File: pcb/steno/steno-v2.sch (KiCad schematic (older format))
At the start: 59 parts, among them J1 Conn_01x02, J2 Conn_01x04, K1 KEYSW, K10 KEYSW, K11 KEYSW, K12 KEYSW, K13 KEYSW, K14 KEYSW, K15 KEYSW, K16 KEYSW, K17 KEYSW, K18 KEYSW, K19 KEYSW, K2 KEYSW, K20 KEYSW, K21 KEYSW, K22 KEYSW, K23 KEYSW, K24 KEYSW, K25 KEYSW, K26 KEYSW, K27 KEYSW, K28 KEYSW, K3 KEYSW, K4 KEYSW, K5 KEYSW, K6 KEYSW, K7 KEYSW, K8 KEYSW, K9 KEYSW, U1 Adafruit_Feather

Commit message: v2 KiCAD files
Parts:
- added D29, D30: DIODE, Diode_THT:D_DO-34_SOD68_P7.62mm_Horizontal, symbol Simulation_SPICE:DIODE
- added J2: 503182-1852, misc:MOLEX_503182-1852, symbol 503182-1852:503182-1852
- added K29, K30: KEYSW, Keebio-Parts:Kailh-PG1350-1u-No-Clickhole, symbol canadian_parts:KEYSW
- added R1: 10K, Resistor_SMD:R_0805_2012Metric, symbol Device:R
- added U2: MT25QL128ABA1ESE, steno:SOIC-8, symbol steno:MT25QL128ABA1ESE
- renumbered J2 to J3
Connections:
- net labels added: COL10, COL7, COL8, COL9, CS, MISO, MOSI, SCLK
- net labels removed: ROW4, ROW5
- wire segments 127 -> 120
- no-connect marks 6 -> 5
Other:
- moved on the sheet: D1, K1

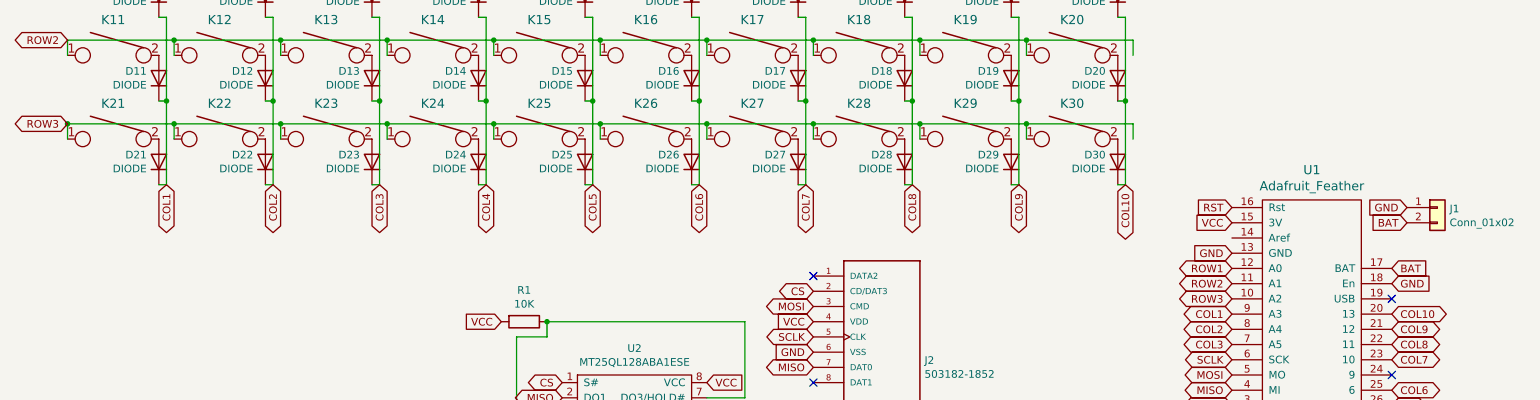
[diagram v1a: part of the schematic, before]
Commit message: Update PCB and footprints
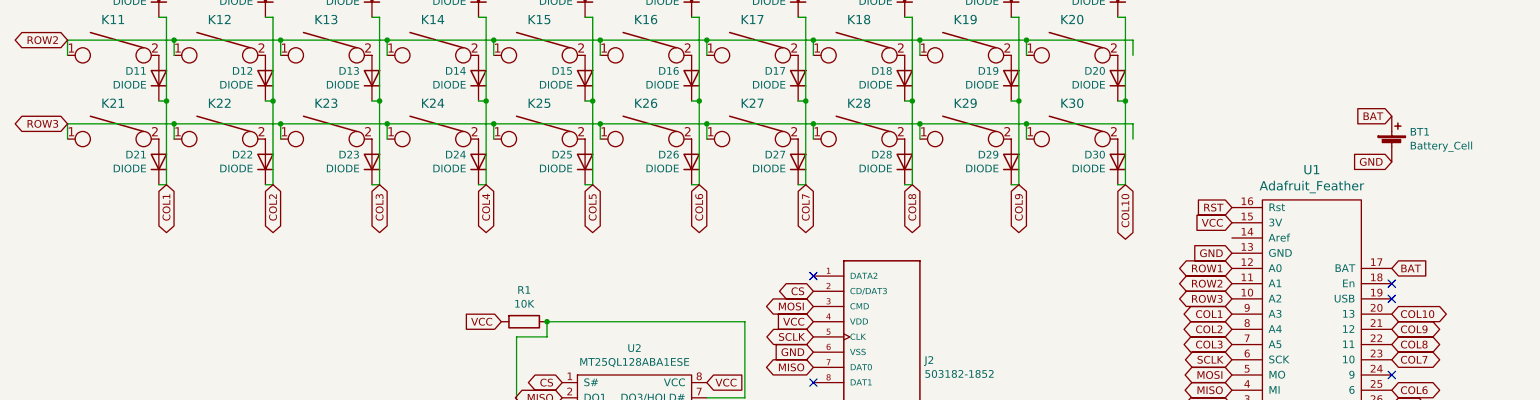
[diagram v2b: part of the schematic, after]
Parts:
- removed J1: Conn_01x02, Connector_JST:JST_PH_B2B-PH-SM4-TB_1x02-1MP_P2.00mm_Vertical, symbol Connector_Generic:Conn_01x02
- added BT1: Battery_Cell, Connector_JST:JST_PH_S2B-PH-SM4-TB_1x02-1MP_P2.00mm_Horizontal, symbol Device:Battery_Cell
- U2: footprint steno:SOIC-8 -> Package_SO:SOP-8_5.28x5.23mm_P1.27mm
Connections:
- no-connect marks 5 -> 6
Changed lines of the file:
@@
 NoConn ~ 9650 5800
 NoConn ~ 10700 4900
-Text GLabel 10700 4800 2    50   Input ~ 0
-GND
-$Comp
-L Connector_Generic:Conn_01x02 J1
-U 1 1 5E6B230F
-P 11000 4300
-F 0 "J1" H 11080 4292 50  0000 L CNN
-F 1 "Conn_01x02" H 11080 4201 50  0000 L CNN
-F 2 "Connector_JST:JST_PH_B2B-PH-SM4-TB_1x02-1MP_P2.00mm_Vertical" H 11000 4300 50  0001 C CNN
-F 3 "~" H 11000 4300 50  0001 C CNN
-	1    11000 4300
-	1    0    0    -1
-$EndComp
-Text GLabel 10800 4300 0    50   Input ~ 0
+Text GLabel 10700 4000 0    50   Input ~ 0
 GND
 Text GLabel 10700 4700 2    50   Input ~ 0
 BAT
-Text GLabel 10800 4400 0    50   Input ~ 0
+Text GLabel 10700 3700 0    50   Input ~ 0
 BAT
 $Comp
@@
 F 0 "U2" H 5725 5875 50  0000 C CNN
 F 1 "MT25QL128ABA1ESE" H 5725 5784 50  0000 C CNN
-F 2 "steno:SOIC-8" H 5650 5150 50  0001 C CNN
+F 2 "Package_SO:SOP-8_5.28x5.23mm_P1.27mm" H 5650 5150 50  0001 C CNN
 F 3 "" H 5650 5150 50  0001 C CNN
 	1    5650 5550
@@
 Wire Wire Line
 	2700 3750 3400 3750
-Connection ~ 2000 3750
+NoConn ~ 10700 4800
+$Comp
+L Device:Battery_Cell BT1
+U 1 1 5EC9EBF8
+P 10700 3900
+F 0 "BT1" H 10818 3996 50  0000 L CNN
+F 1 "Battery_Cell" H 10818 3905 50  0000 L CNN
+F 2 "Connector_JST:JST_PH_S2B-PH-SM4-TB_1x02-1MP_P2.00mm_Horizontal" V 10700 3960 50  0001 C CNN
+F 3 "~" V 10700 3960 50  0001 C CNN
+	1    10700 3900
+	1    0    0    -1
+$EndComp
 $EndSCHEMATC

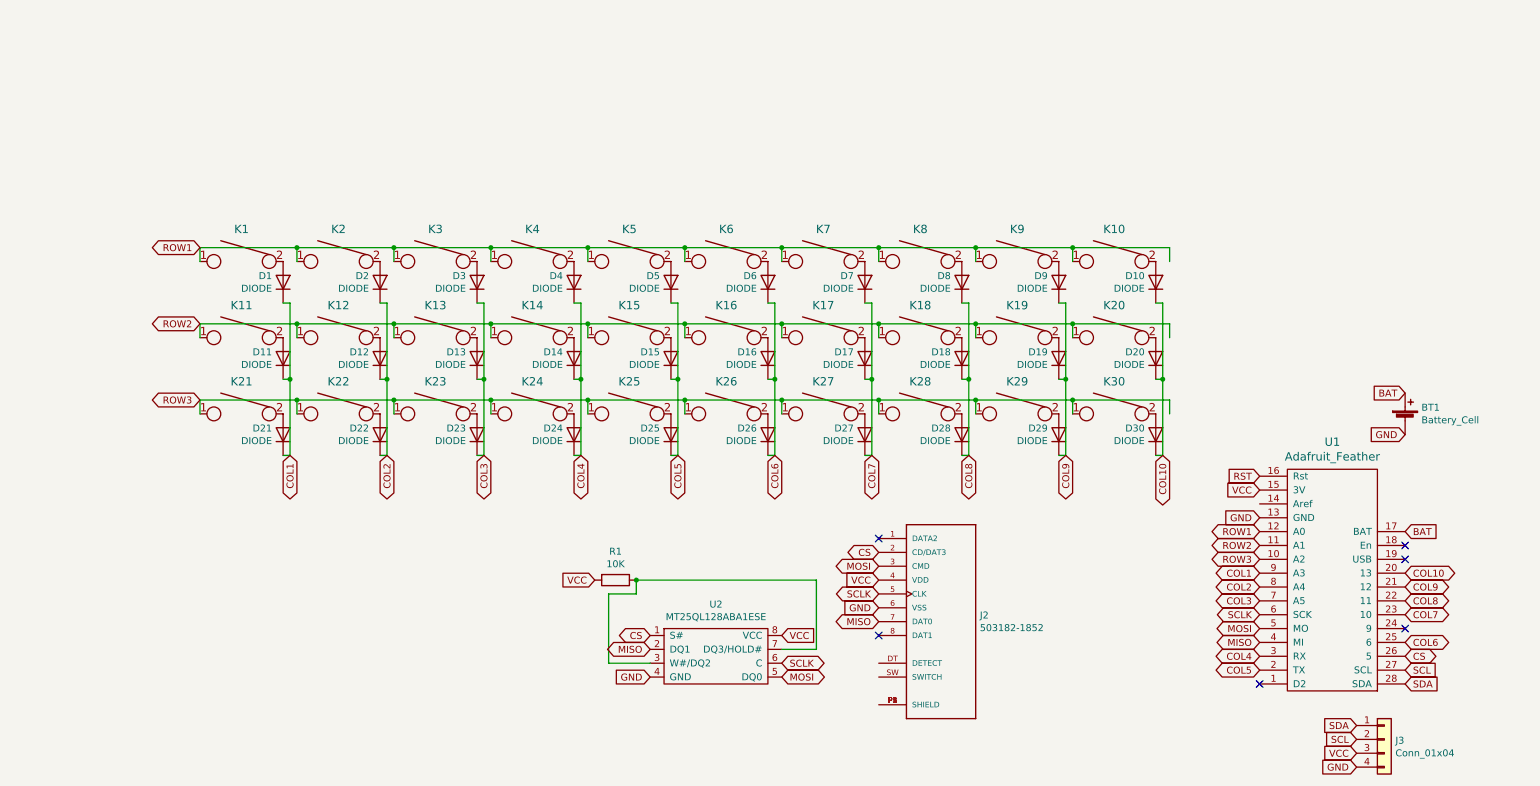
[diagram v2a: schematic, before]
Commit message: v3 component placement; Removed JST connector; Added OLED footprint
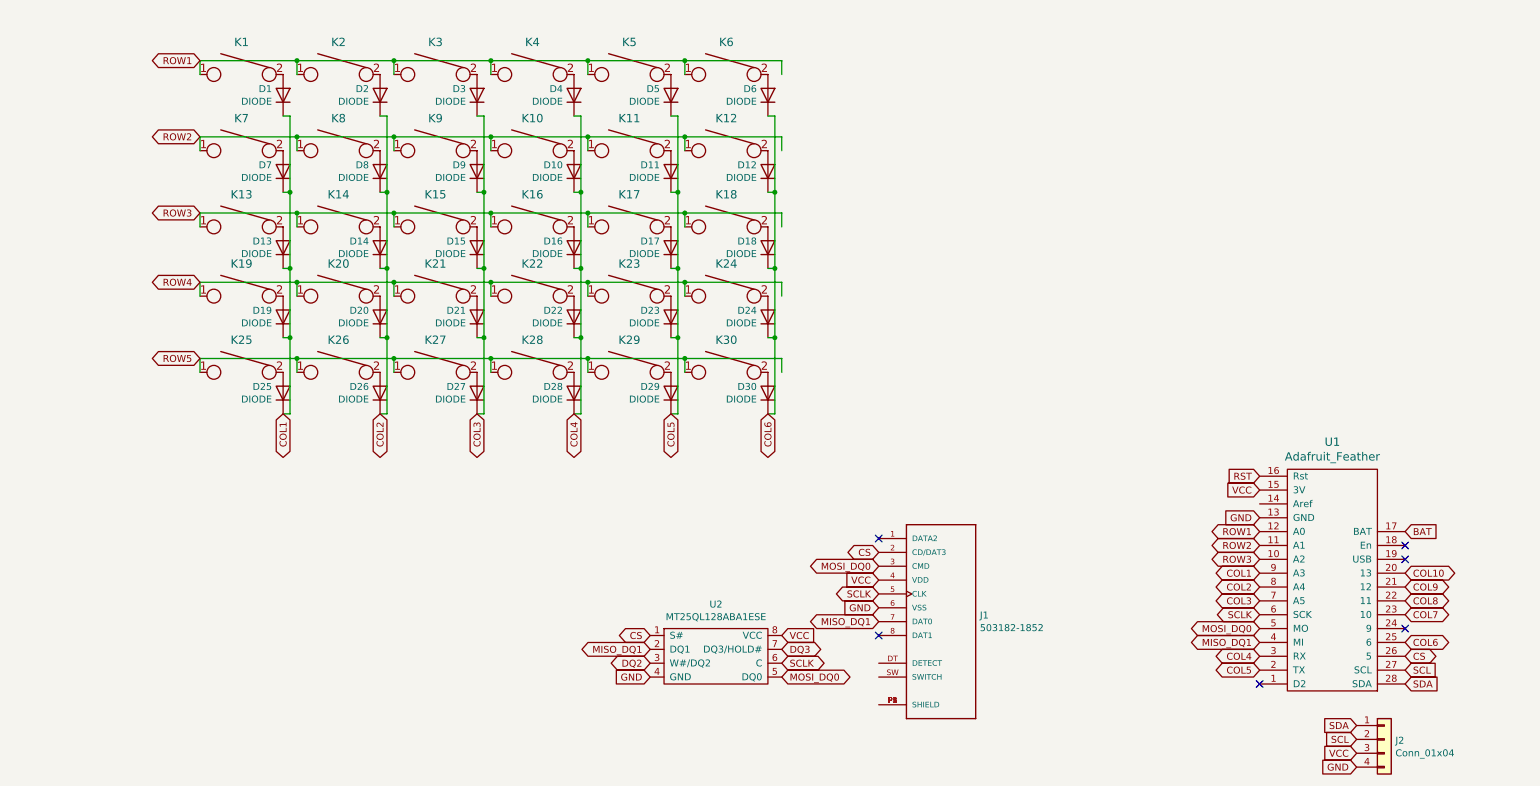
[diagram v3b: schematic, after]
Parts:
- removed BT1: Battery_Cell, Connector_JST:JST_PH_S2B-PH-SM4-TB_1x02-1MP_P2.00mm_Horizontal, symbol Device:Battery_Cell
- removed D10, D16, D17, D7, D8, D9: DIODE, Diode_THT:D_DO-34_SOD68_P7.62mm_Horizontal, symbol Simulation_SPICE:DIODE
- removed K10, K16, K17, K7, K8, K9: KEYSW, Keebio-Parts:Kailh-PG1350-1u-No-Clickhole, symbol canadian_parts:KEYSW
- removed R1: 10K, Resistor_SMD:R_0805_2012Metric, symbol Device:R
- added D12, D21, D22, D23, D24, D25: DIODE, Diode_THT:D_DO-34_SOD68_P7.62mm_Horizontal, symbol Simulation_SPICE:DIODE
- added K12, K21, K22, K23, K24, K25: KEYSW, Keebio-Parts:Kailh-PG1350-1u-No-Clickhole, symbol canadian_parts:KEYSW
- J2: renamed from J3; footprint Connector_PinHeader_2.54mm:PinHeader_1x04_P2.54mm_Vertical -> steno:OLED
- renumbered D14 to D10, D15 to D11, D21 to D13, D22 to D14, D23 to D15, D24 to D16, D25 to D17, D11 to D7, D12 to D8, D13 to D9, J2 to J1, K14 to K10, K15 to K11, K21 to K13, K22 to K14, K23 to K15, K24 to K16, K25 to K17, K11 to K7, K12 to K8, K13 to K9
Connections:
- net labels added: DQ2, DQ3, MISO_DQ1, MOSI_DQ0, ROW4, ROW5
- net labels removed: MISO, MOSI
- wire segments 120 -> 119
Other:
- moved on the sheet: D1, D10, D11, D13, D14, D15, D16, D17, D2, D3, D4, D5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

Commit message: Routed and plotted v3
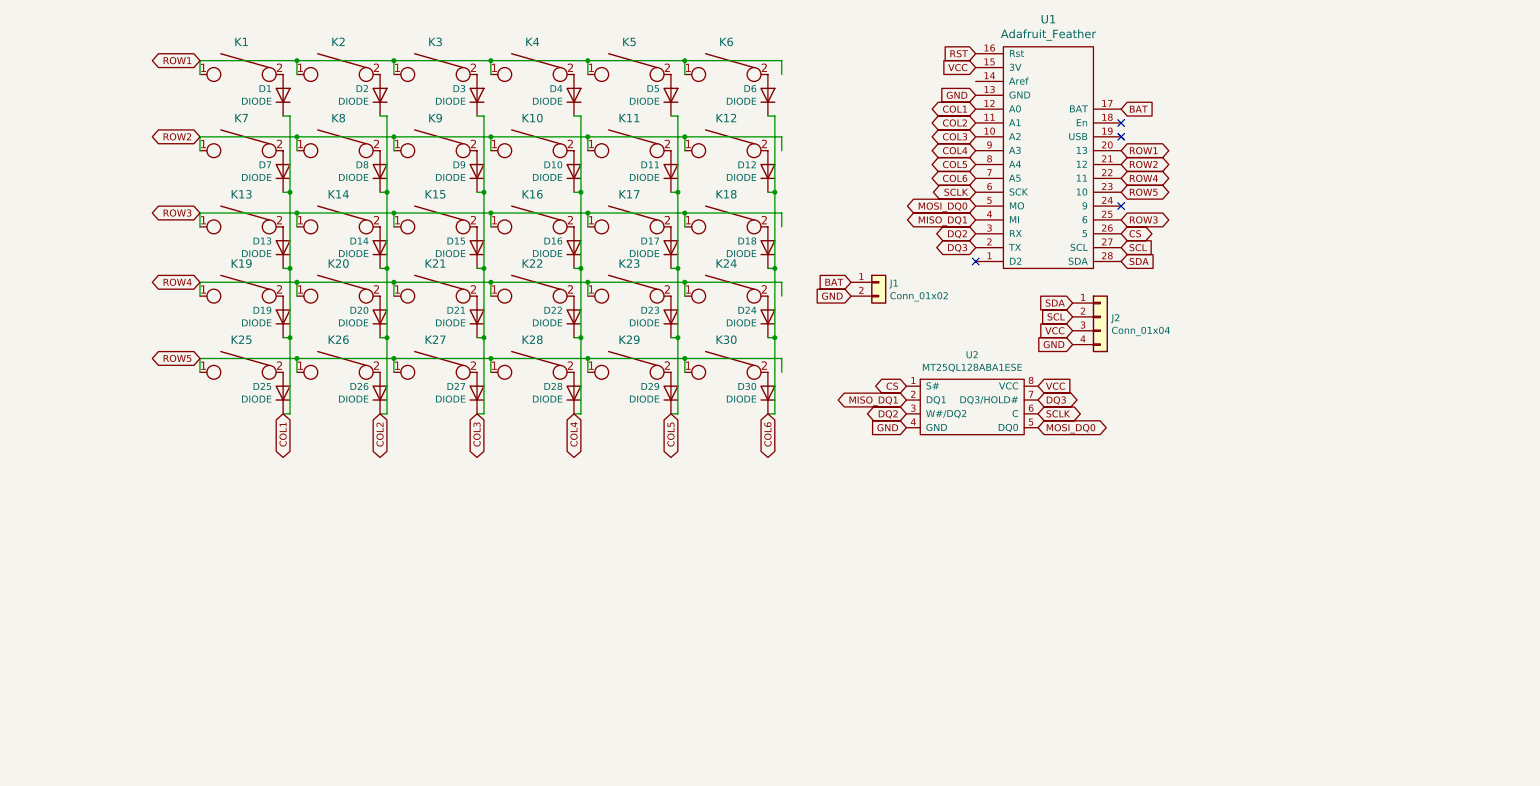
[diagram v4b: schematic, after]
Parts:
- removed J1: 503182-1852, misc:MOLEX_503182-1852, symbol 503182-1852:503182-1852
- added J1: Conn_01x02, Connector_PinHeader_2.54mm:PinHeader_1x02_P2.54mm_Vertical, symbol Connector_Generic:Conn_01x02
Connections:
- net labels removed: COL10, COL7, COL8, COL9
- no-connect marks 6 -> 4
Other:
- moved on the sheet: J2, U1, U2
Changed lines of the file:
@@
 	0    -1   1    0
 $EndComp
-Text GLabel 9650 4600 0    50   Input ~ 0
+Text GLabel 7600 1550 0    50   Input ~ 0
 GND
-Text GLabel 9650 4700 0    50   BiDi ~ 0
+Text GLabel 8650 1950 2    50   BiDi ~ 0
 ROW1
-Text GLabel 9650 4800 0    50   BiDi ~ 0
+Text GLabel 8650 2050 2    50   BiDi ~ 0
 ROW2
-Text GLabel 9650 4900 0    50   BiDi ~ 0
+Text GLabel 8650 2450 2    50   BiDi ~ 0
 ROW3
-Text GLabel 9650 5600 0    50   BiDi ~ 0
+Text GLabel 7600 1950 0    50   BiDi ~ 0
 COL4
-Text GLabel 9650 5700 0    50   BiDi ~ 0
+Text GLabel 7600 2050 0    50   BiDi ~ 0
 COL5
-Text GLabel 9650 4300 0    50   Input ~ 0
+Text GLabel 7600 1250 0    50   Input ~ 0
 RST
-Text GLabel 9650 5200 0    50   BiDi ~ 0
+Text GLabel 7600 1850 0    50   BiDi ~ 0
 COL3
-Text GLabel 9650 5100 0    50   BiDi ~ 0
+Text GLabel 7600 1750 0    50   BiDi ~ 0
 COL2
-Text GLabel 9650 5000 0    50   BiDi ~ 0
+Text GLabel 7600 1650 0    50   BiDi ~ 0
 COL1
-Text GLabel 10700 5500 2    50   BiDi ~ 0
+Text GLabel 7600 2150 0    50   BiDi ~ 0
 COL6
-NoConn ~ 10700 5400
-NoConn ~ 9650 5800
-NoConn ~ 10700 4900
-Text GLabel 10700 4700 2    50   Input ~ 0
+NoConn ~ 8650 2350
+NoConn ~ 7600 2750
+NoConn ~ 8650 1850
+Text GLabel 8650 1650 2    50   Input ~ 0
 BAT
 $Comp
 L steno-rescue:Adafruit_Feather-ProMicro U1
 U 1 1 5E4CA943
-P 10150 4650
-F 0 "U1" H 10175 5247 60  0000 C CNN
-F 1 "Adafruit_Feather" H 10175 5141 60  0000 C CNN
-F 2 "Downloads:ADAFRUIT_FEATHER" H 10150 4650 60  0001 C CNN
-F 3 "" H 10150 4650 60  0001 C CNN
-	1    10150 4650
+P 8100 1600
+F 0 "U1" H 8125 2197 60  0000 C CNN
+F 1 "Adafruit_Feather" H 8125 2091 60  0000 C CNN
+F 2 "Downloads:ADAFRUIT_FEATHER" H 8100 1600 60  0001 C CNN
+F 3 "" H 8100 1600 60  0001 C CNN
+	1    8100 1600
 	1    0    0    -1
 $EndComp
@@
 L Connector_Generic:Conn_01x04 J2
 U 1 1 5EB05CC7
-P 10550 6200
-F 0 "J2" H 10630 6192 50  0000 L CNN
-F 1 "Conn_01x04" H 10630 6101 50  0000 L CNN
-F 2 "steno:OLED" H 10550 6200 50  0001 C CNN
-F 3 "~" H 10550 6200 50  0001 C CNN
-	1    10550 6200
+P 8500 3150
+F 0 "J2" H 8580 3142 50  0000 L CNN
+F 1 "Conn_01x04" H 8580 3051 50  0000 L CNN
+F 2 "steno:OLED" H 8500 3150 50  0001 C CNN
+F 3 "~" H 8500 3150 50  0001 C CNN
+	1    8500 3150
 	1    0    0    -1
 $EndComp
-Text GLabel 10700 5700 2    50   Input ~ 0
+Text GLabel 8650 2650 2    50   Input ~ 0
 SCL
-Text GLabel 10700 5800 2    50   Input ~ 0
+Text GLabel 8650 2750 2    50   Input ~ 0
 SDA
-Text GLabel 10350 6100 0    50   Input ~ 0
+Text GLabel 8300 3050 0    50   Input ~ 0
 SDA
-Text GLabel 10350 6200 0    50   Input ~ 0
+Text GLabel 8300 3150 0    50   Input ~ 0
 SCL
-Text GLabel 10350 6400 0    50   Input ~ 0
+Text GLabel 8300 3350 0    50   Input ~ 0
 GND
-Text GLabel 9650 4400 0    50   Input ~ 0
+Text GLabel 7600 1350 0    50   Input ~ 0
 VCC
-Text GLabel 10350 6300 0    50   Input ~ 0
+Text GLabel 8300 3250 0    50   Input ~ 0
 VCC
 Text GLabel 2000 1850 0    50   BiDi ~ 0
@@
 Text GLabel 2000 2400 0    50   BiDi ~ 0
 ROW3
-Text GLabel 10700 5300 2    50   BiDi ~ 0
-COL7
-Text GLabel 10700 5200 2    50   BiDi ~ 0
-COL8
-Text GLabel 10700 5100 2    50   BiDi ~ 0
-COL9
-Text GLabel 10700 5000 2    50   BiDi ~ 0
-COL10
 $Comp
 L steno:MT25QL128ABA1ESE U2
 U 1 1 5ECCCE62
-P 5650 5550
-F 0 "U2" H 5725 5875 50  0000 C CNN
-F 1 "MT25QL128ABA1ESE" H 5725 5784 50  0000 C CNN
-F 2 "Package_SO:SOP-8_5.28x5.23mm_P1.27mm" H 5650 5150 50  0001 C CNN
-F 3 "" H 5650 5150 50  0001 C CNN
-	1    5650 5550
+P 7500 3750
+F 0 "U2" H 7575 4075 50  0000 C CNN
+F 1 "MT25QL128ABA1ESE" H 7575 3984 50  0000 C CNN
+F 2 "Package_SO:SOP-8_5.28x5.23mm_P1.27mm" H 7500 3350 50  0001 C CNN
+F 3 "" H 7500 3350 50  0001 C CNN
+	1    7500 3750
 	1    0    0    -1
 $EndComp
-Text GLabel 6900 5050 0    50   Input ~ 0
+Text GLabel 8050 3650 2    50   Input ~ 0
 VCC
-Text GLabel 6200 5450 2    50   Input ~ 0
-VCC
-Text GLabel 6900 5250 0    50   Input ~ 0
+Text GLabel 7100 3950 0    50   Input ~ 0
 GND
-Text GLabel 5250 5750 0    50   Input ~ 0
-GND
-Text GLabel 10700 5600 2    50   BiDi ~ 0
+Text GLabel 8650 2550 2    50   BiDi ~ 0
 CS
-Text GLabel 6900 4850 0    50   BiDi ~ 0
+Text GLabel 7600 2250 0    50   BiDi ~ 0
+SCLK
+Text GLabel 7100 3650 0    50   BiDi ~ 0
 CS
-Text GLabel 9650 5300 0    50   BiDi ~ 0
+Text GLabel 8050 3850 2    50   BiDi ~ 0
 SCLK
-Text GLabel 6900 5150 0    50   BiDi ~ 0
-SCLK
-NoConn ~ 6900 5450
-NoConn ~ 6900 4750
-Text GLabel 5250 5450 0    50   BiDi ~ 0
-CS
-Text GLabel 6200 5650 2    50   BiDi ~ 0
-SCLK
-Text GLabel 5250 5550 0    50   BiDi ~ 0
+Text GLabel 7100 3750 0    50   BiDi ~ 0
 MISO_DQ1
-$Comp
-L 503182-1852:503182-1852 J1
-U 1 1 5ED2196F
-P 7100 5350
-F 0 "J1" H 7630 5396 50  0000 L CNN
-F 1 "503182-1852" H 7630 5305 50  0000 L CNN
-F 2 "misc:MOLEX_503182-1852" H 7100 5350 50  0001 L BNN
-F 3 "Molex" H 7100 5350 50  0001 L BNN
-	1    7100 5350
-	1    0    0    -1
-$EndComp
 Wire Wire Line
 	2000 2500 2000 2400
@@
 Wire Wire Line
 	2700 2400 3400 2400
-NoConn ~ 10700 4800
+NoConn ~ 8650 1750
 $Comp
 L canadian_parts:KEYSW K6
@@
 Connection ~ 2650 3300
 Connection ~ 2650 2800
-Text GLabel 6200 5750 2    50   BiDi ~ 0
+Text GLabel 8050 3950 2    50   BiDi ~ 0
 MOSI_DQ0
-Text GLabel 6200 5550 2    50   BiDi ~ 0
+Text GLabel 8050 3750 2    50   BiDi ~ 0
 DQ3
-Text GLabel 5250 5650 0    50   BiDi ~ 0
+Text GLabel 7100 3850 0    50   BiDi ~ 0
 DQ2
-Text GLabel 9650 5400 0    50   BiDi ~ 0
+Text GLabel 7600 2350 0    50   BiDi ~ 0
 MOSI_DQ0
-Text GLabel 9650 5500 0    50   BiDi ~ 0
+Text GLabel 7600 2450 0    50   BiDi ~ 0
 MISO_DQ1
 Text GLabel 2600 3850 3    50   BiDi ~ 0
@@
 Text GLabel 6100 3850 3    50   BiDi ~ 0
 COL6
-Text GLabel 6900 5350 0    50   BiDi ~ 0
-MISO_DQ1
-Text GLabel 6900 4950 0    50   BiDi ~ 0
-MOSI_DQ0
+Text GLabel 8650 2150 2    50   BiDi ~ 0
+ROW4
+Text GLabel 8650 2250 2    50   BiDi ~ 0
+ROW5
+Text GLabel 7600 2550 0    50   BiDi ~ 0
+DQ2
+Text GLabel 7600 2650 0    50   BiDi ~ 0
+DQ3
+$Comp
+L Connector_Generic:Conn_01x02 J1
+U 1 1 5F177638
+P 6900 2900
+F 0 "J1" H 6980 2892 50  0000 L CNN
+F 1 "Conn_01x02" H 6980 2801 50  0000 L CNN
+F 2 "Connector_PinHeader_2.54mm:PinHeader_1x02_P2.54mm_Vertical" H 6900 2900 50  0001 C CNN
+F 3 "~" H 6900 2900 50  0001 C CNN
+	1    6900 2900
+	1    0    0    -1
+$EndComp
+Text GLabel 6700 2900 0    50   Input ~ 0
+BAT
+Text GLabel 6700 3000 0    50   Input ~ 0
+GND
 $EndSCHEMATC
